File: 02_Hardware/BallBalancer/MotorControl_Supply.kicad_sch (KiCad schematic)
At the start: 55 parts, among them J6 Jack-DC, M1 Motor_DC, M2 Motor_DC, Q1 DMN10H220L, Q2 DMN10H220L, Q3 DMN10H220L, Q4 DMN10H220L, Q5 DMN10H220L, Q6 DMN10H220L, Q7 DMN10H220L, Q8 DMN10H220L, U4 DGD0506A, U5 DGD0506A, U6 AP63203WU, U6 DGD0506A, U7 DGD0506A, U8 LP2985-5.0

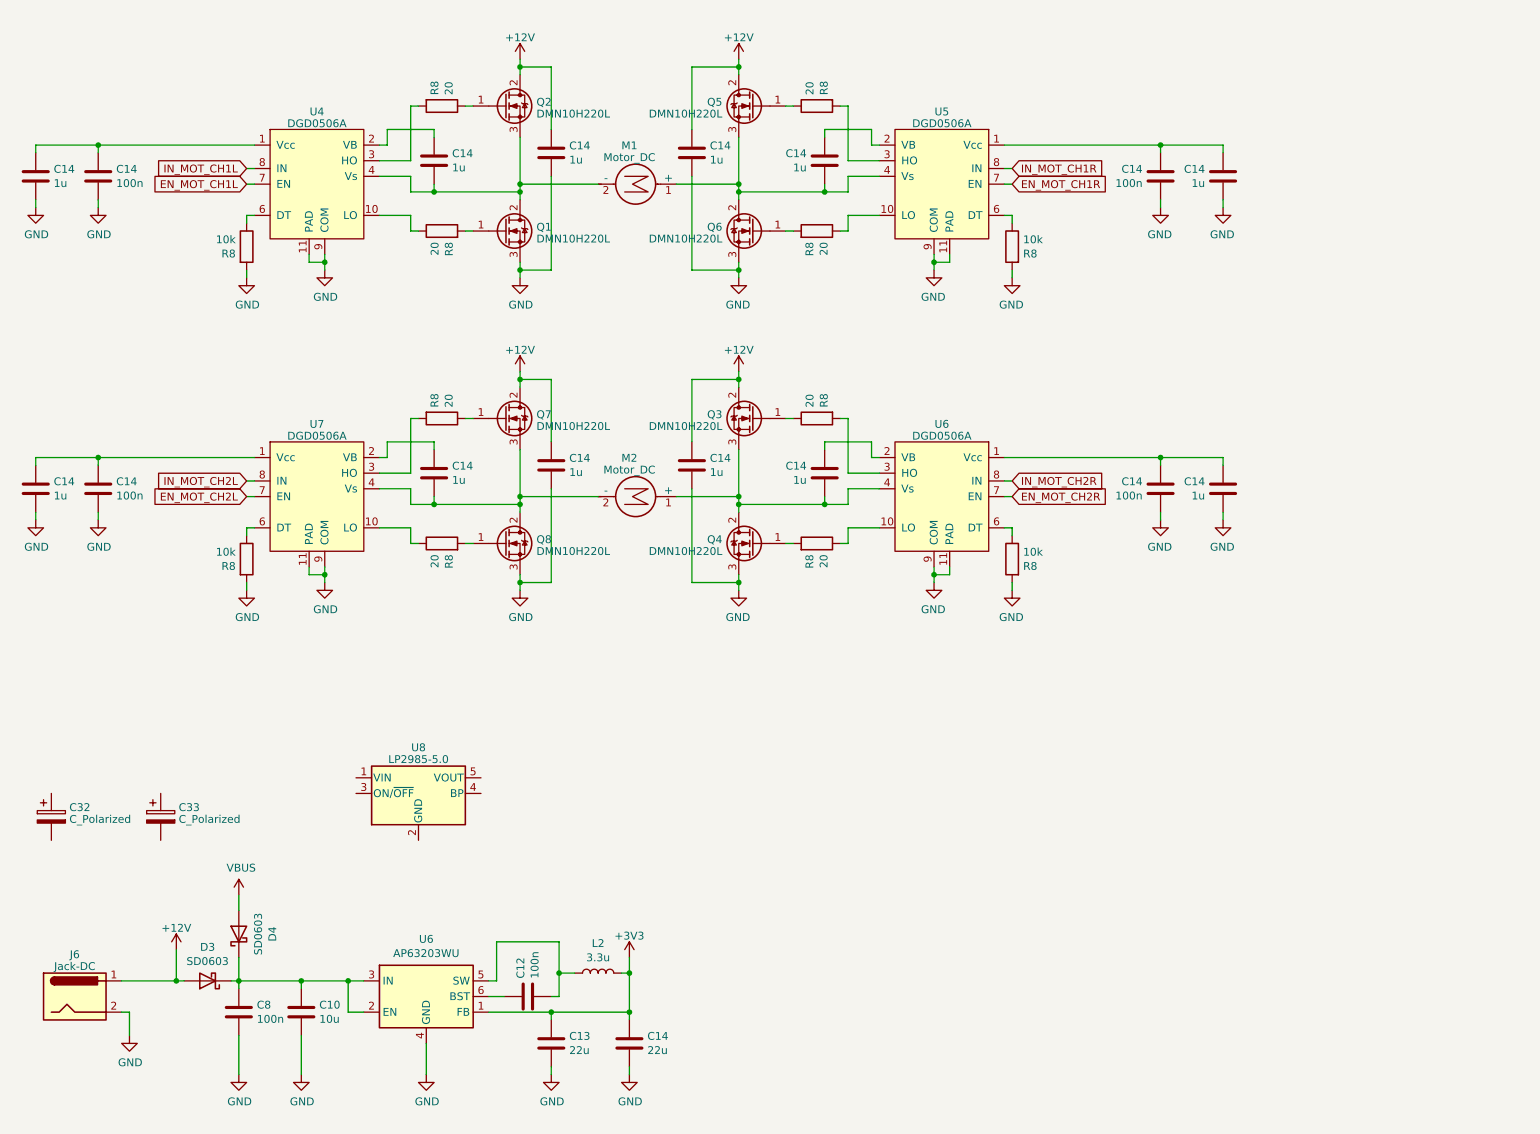
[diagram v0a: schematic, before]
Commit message: Hardware schema and layout created
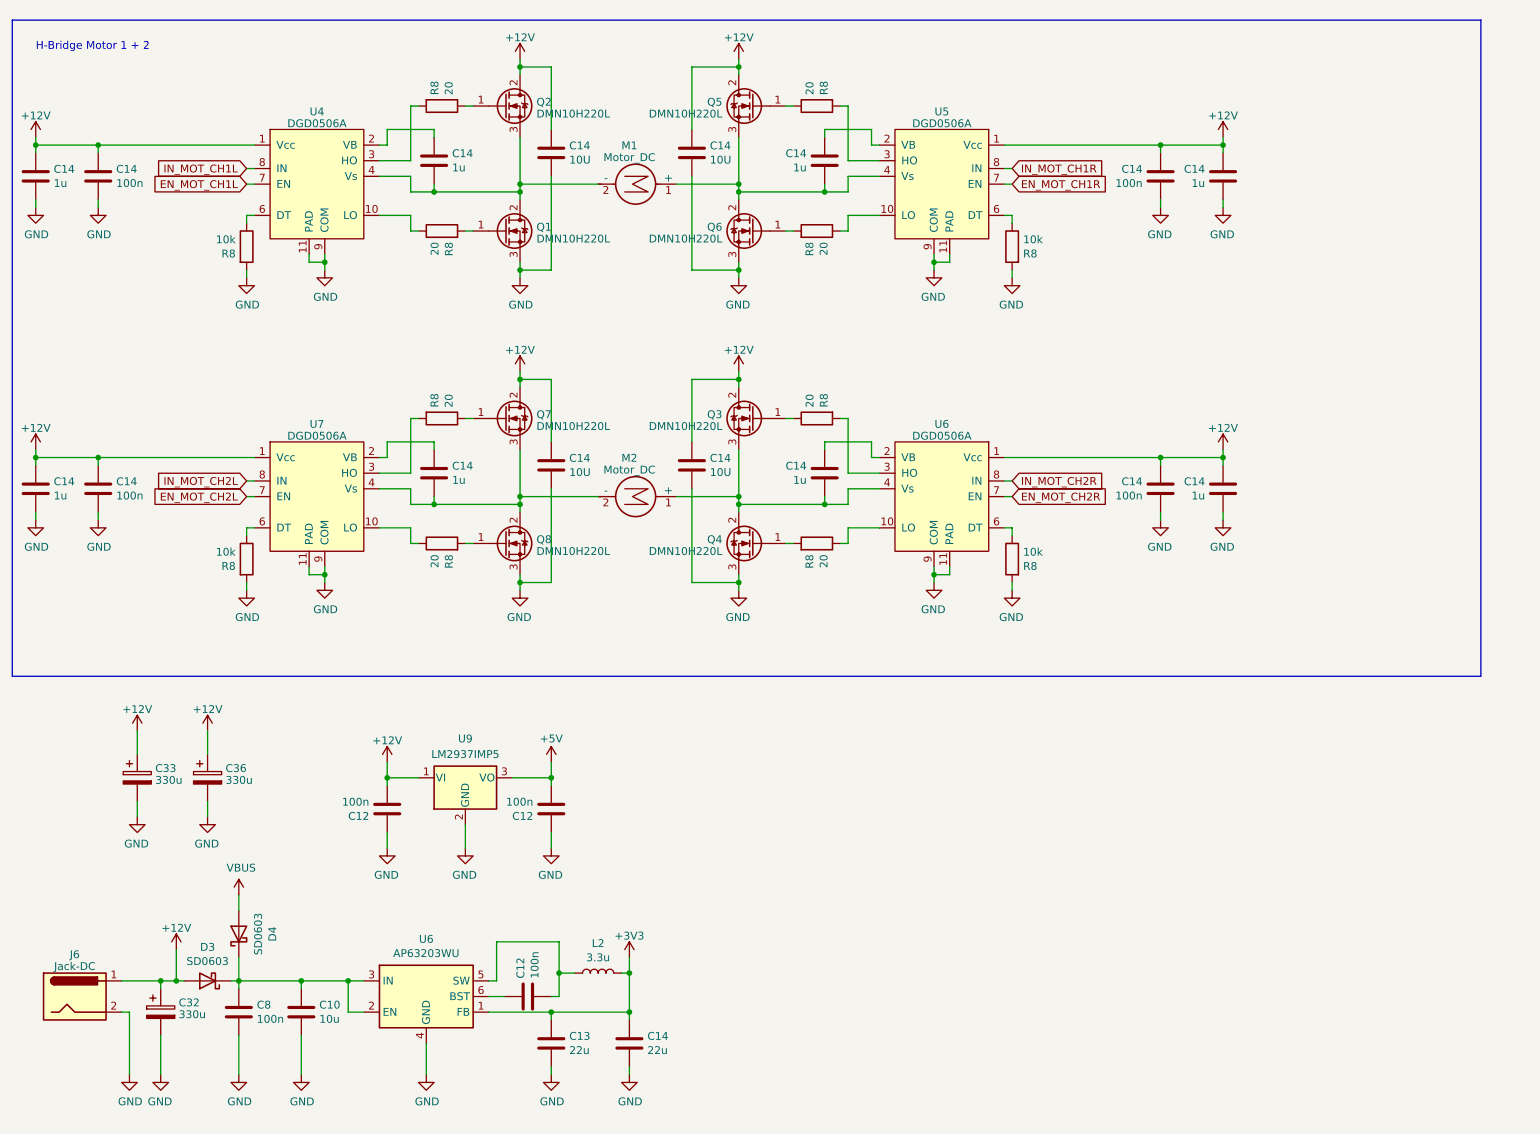
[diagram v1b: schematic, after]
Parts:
- removed U8: LP2985-5.0, Package_TO_SOT_SMD:SOT-23-5, symbol Regulator_Linear:LP2985-5.0
- added C12 (x2): 100n, Capacitor_SMD:C_0603_1608Metric, symbol Device:C
- added C36: 330u, Capacitor_SMD:CP_Elec_8x10, symbol Device:C_Polarized
- added U9: LM2937IMP5, Package_TO_SOT_SMD:SOT-223-3_TabPin2, symbol Regulator_Linear:LM2937xMP
- C14: footprint Capacitor_SMD:C_0603_1608Metric -> Capacitor_SMD:C_0805_2012Metric
- C14: value 1u -> 10U; footprint Capacitor_SMD:C_0603_1608Metric -> Capacitor_SMD:C_1210_3225Metric
- C32, C33: value C_Polarized -> 330u; footprint (none) -> Capacitor_SMD:CP_Elec_8x10
- J6: footprint (none) -> Connector_BarrelJack:BarrelJack_CUI_PJ-063AH_Horizontal
- M1, M2: footprint (none) -> Connector_PinHeader_2.54mm:PinHeader_1x02_P2.54mm_Vertical
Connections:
- net +12V: now also C14.2, C14.2, C14.2, C14.2, C14.2, C14.2, C14.2, C14.2, C32.1, C33.1, U4.1 (Vcc), U5.1 (Vcc), U6.1 (Vcc), U7.1 (Vcc), C12.1, C36.1, U9.1 (VI)
- net GND: now also C32.2, C33.2, C12.2, C12.2, C36.2, U9.2 (GND)
- new net +5V: C12.1, U9.3 (VO)
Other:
- note added: "H-Bridge Motor 1 + 2"
- moved on the sheet: C32

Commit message: ERC and DRC warnings and errors in schema and layout fixed
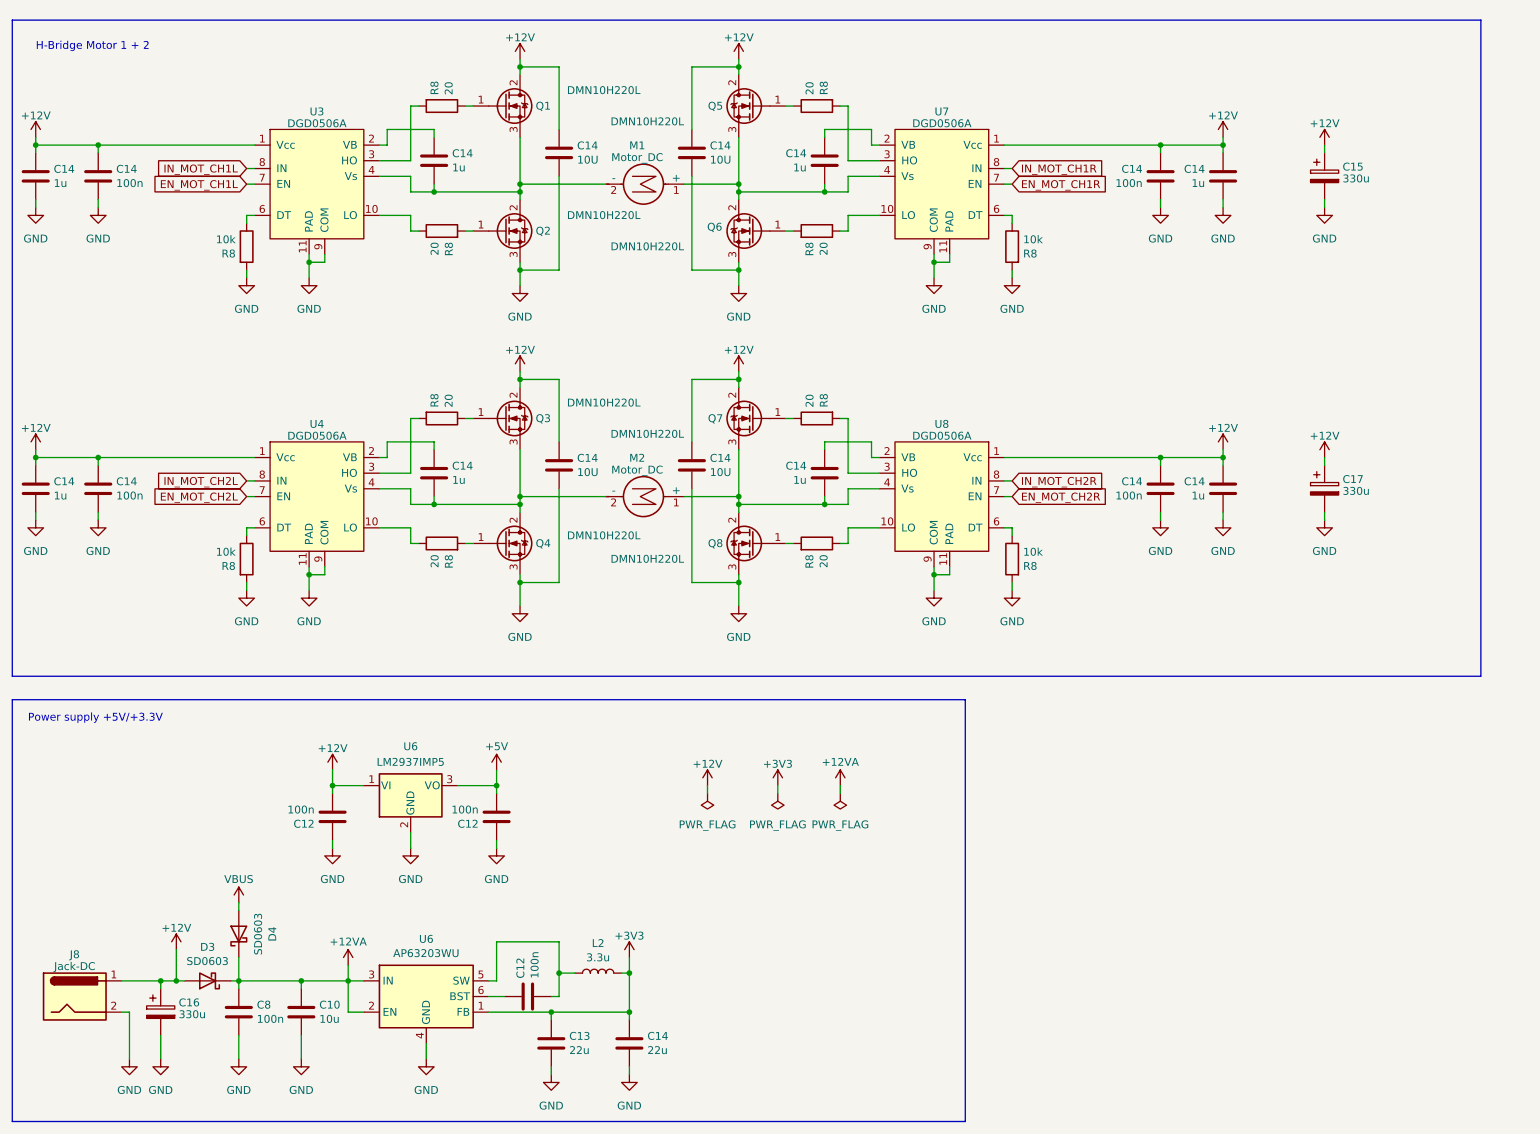
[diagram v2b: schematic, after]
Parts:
- renumbered C33 to C15, C32 to C16, C36 to C17, J6 to J8, Q2 to Q1, Q1 to Q2, Q7 to Q3, Q8 to Q4, Q3 to Q7, Q4 to Q8, U4 to U3, U7 to U4, U9 to U6, U5 to U7, U6 to U8
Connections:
- net +12VA: now reaches C10.1, C8.1, D3.1 (K), D4.1 (K), U6.2 (EN), U6.3 (IN)
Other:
- note added: "Power supply +5V/+3.3V"
- moved on the sheet: C12, C14, C15, C17, M1, M2, U6

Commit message: Test points added and BOM created
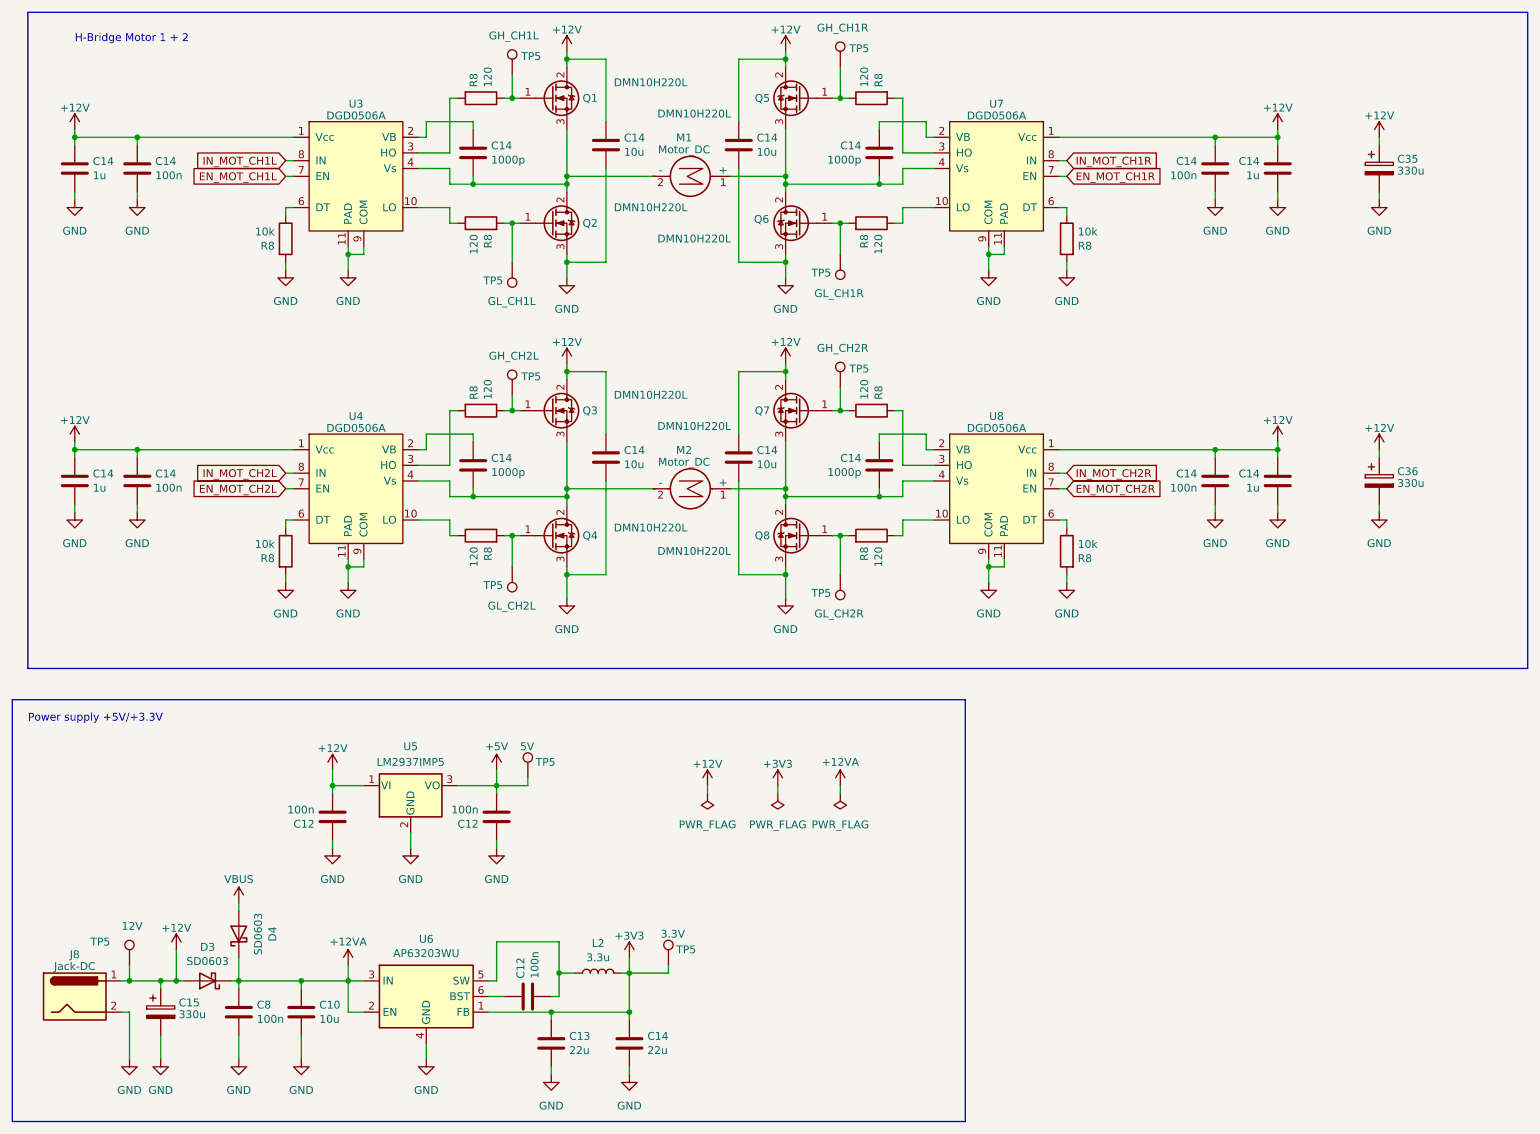
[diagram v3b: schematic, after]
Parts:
- added TP5: 5V, TestPoint:TestPoint_Pad_D1.0mm, symbol Connector:TestPoint
- added TP5: GL_CH1R, TestPoint:TestPoint_Pad_D1.0mm, symbol Connector:TestPoint
- added TP5: GH_CH2R, TestPoint:TestPoint_Pad_D1.0mm, symbol Connector:TestPoint
- added TP5: 3.3V, TestPoint:TestPoint_Pad_D1.0mm, symbol Connector:TestPoint
- added TP5: GH_CH2L, TestPoint:TestPoint_Pad_D1.0mm, symbol Connector:TestPoint
- added TP5: GL_CH2L, TestPoint:TestPoint_Pad_D1.0mm, symbol Connector:TestPoint
- added TP5: 12V, TestPoint:TestPoint_Pad_D1.0mm, symbol Connector:TestPoint
- added TP5: GH_CH1L, TestPoint:TestPoint_Pad_D1.0mm, symbol Connector:TestPoint
- added TP5: GL_CH2R, TestPoint:TestPoint_Pad_D1.0mm, symbol Connector:TestPoint
- added TP5: GH_CH1R, TestPoint:TestPoint_Pad_D1.0mm, symbol Connector:TestPoint
- added TP5: GL_CH1L, TestPoint:TestPoint_Pad_D1.0mm, symbol Connector:TestPoint
- C10: footprint Capacitor_SMD:C_0603_1608Metric -> Capacitor_SMD:C_0805_2012Metric; Hersteller Nr. GRM188R6YA106MA73D -> C2012X5R1V106K085AC; Info (none) -> 10uF; 35V; X5R; -55C; +85C; Mouser Nr. 81-GRM188R6YA106MA3D -> 810-C2012X5R1V106K0C
- C12, C8: Hersteller Nr. CL10B104KB8NNWC -> 885382206004; Info (none) -> 0.1uF; 50V, X7R; -55C;+125C; Mouser Nr. 187-CL10B104KB8NNWC -> 710-885382206004
- C13, C14: Info (none) -> 22uF; 16V; X5R; -55C; +85C
- C14: Hersteller Nr. (none) -> CL10B105KA8NNNC; Info (none) -> 1uF; 25V;X7R; -55C;+125C; Mouser Nr. (none) -> 187-CL10B105KA8NNNC
- C14: value 1u -> 1000p; Hersteller Nr. (none) -> C0805J102K5RACAUTO; Info (none) -> 1000pF; 50V; X7R; -55C; +125C; Mouser Nr. (none) -> 80-C0805J102K5RAUTO
- C14: Hersteller Nr. (none) -> 885382206004; Info (none) -> 0.1uF; 50V, X7R; -55C;+125C; Mouser Nr. (none) -> 710-885382206004
- C14: value 10U -> 10u; Hersteller Nr. (none) -> CL32B106KMVNNWE; Info (none) -> 10uF; 63V; X7R; -55C; +125C; Mouser Nr. (none) -> 187-CL32B106KMVNNWE
- C15: renamed from C16; Hersteller Nr. (none) -> UWT1E331MNL1GS; Info (none) -> 330uF; 25V; -55C; +105C; ALU; Mouser Nr. (none) -> 647-UWT1E331MNL1S
- C35: renamed from C15; Hersteller Nr. (none) -> UWT1E331MNL1GS; Info (none) -> 330uF; 25V; -55C; +105C; ALU; Mouser Nr. (none) -> 647-UWT1E331MNL1S
- C36: renamed from C17; Hersteller Nr. (none) -> UWT1E331MNL1GS; Info (none) -> 330uF; 25V; -55C; +105C; ALU; Mouser Nr. (none) -> 647-UWT1E331MNL1S
- D3, D4: Info (none) -> 200mA; 450mV; Mouser Nr. 581-SD0603S040S0R2 -> 581-SD0603S040S0R2
- L2: Info (none) -> 3.3uH; 800mA; 80mOhms; Mouser Nr. IMC0805ER3R3J01 -> 70-IMC0805ER3R3J01
- Q1, Q2, Q3, Q4, Q5, Q6, Q7, Q8: Hersteller Nr. (none) -> DMN10H220LK3-13; Info (none) -> N-Channel; 100V; 7.5A; 220mOhms; Mouser Nr. (none) -> 621-DMN10H220LK3-13
- R8: value 20 -> 120; Hersteller Nr. (none) -> CRCW0603120RFKEAC; Info (none) -> 75V; 1%; 100mW; -55C; +155C; Mouser Nr. (none) -> 71-CRCW0603120RFKEA
- R8: Hersteller Nr. (none) -> CRCW060310K0FKEAC; Info (none) -> 75V; 1%; 100mW; -55C; +155C; Mouser Nr. (none) -> 71-CRCW060310K0FKEAC
- U3, U4, U7, U8: Hersteller Nr. (none) -> DGD0506AM10-13; Mouser Nr. (none) -> 621-DGD0506AM10-13
- U5: renamed from U6; Hersteller Nr. (none) -> LM2937IMP-5.0/NOPB; Info (none) -> 5V LDO; Mouser Nr. (none) -> 926-LM2937IMP5.0NOPB
- U6: Info (none) -> 3.3V Buck Converter
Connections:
- net +12V: now also TP5.1
- net +3V3: now also TP5.1
- net +5V: now also TP5.1
- net at Q2.1 (G), R8.2: now also TP5.1
- net at Q6.1 (G), R8.2: now also TP5.1
- net at Q1.1 (G), R8.1: now also TP5.1
- net at Q4.1 (G), R8.2: now also TP5.1
- net at Q8.1 (G), R8.2: now also TP5.1
- net at Q5.1 (G), R8.1: now also TP5.1
- net at Q7.1 (G), R8.1: now also TP5.1
- net at Q3.1 (G), R8.1: now also TP5.1
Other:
- moved on the sheet: C14, C35, C36, M1, M2, Q1, Q2, Q3, Q4, Q5, Q6, Q7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
